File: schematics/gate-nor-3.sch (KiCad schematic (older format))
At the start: 5 parts, among them Q15 NPN

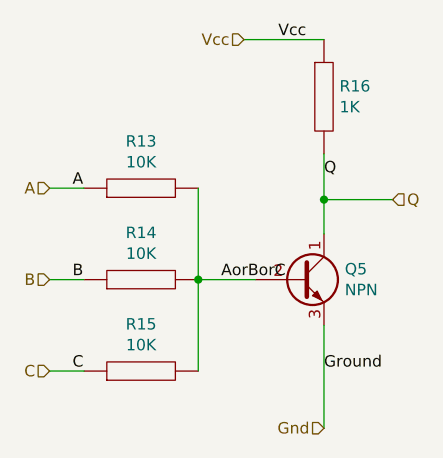
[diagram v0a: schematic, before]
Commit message: Fleshes out basic schematics and some utility software
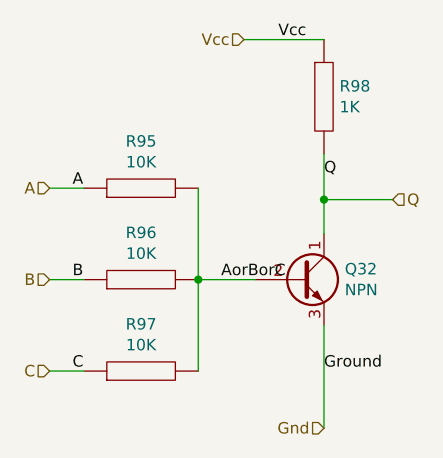
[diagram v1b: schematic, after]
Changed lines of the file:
@@
 EESchema Schematic File Version 4
-LIBS:flip-flop-d-test-cache
 EELAYER 26 0
 EELAYER END
 $Descr A4 11693 8268
 encoding utf-8
-Sheet 20 9
+Sheet 20 50
 Title ""
 Date ""
@@
 AR Path="/5C401646/5C3679F2" Ref="R4"  Part="1"
 AR Path="/5C3FF380/5C403563/5C3679F2" Ref="R16"  Part="1"
-F 0 "R16" H 4268 2546 50  0000 L CNN
+AR Path="/5C4196B1/5C3FF380/5C403563/5C3679F2" Ref="R?"  Part="1"
+AR Path="/5C4199A8/5C403563/5C3679F2" Ref="R?"  Part="1"
+AR Path="/5C41AA0E/5C41AA96/5C3679F2" Ref="R10"  Part="1"
+AR Path="/5C41AA0E/5C41B943/5C3679F2" Ref="R17"  Part="1"
+AR Path="/5C42CE9C/5C41AA0E/5C41AA96/5C3679F2" Ref="R?"  Part="1"
+AR Path="/5C42CE9C/5C41AA0E/5C41B943/5C3679F2" Ref="R?"  Part="1"
+AR Path="/5C42D2B6/5C41AA96/5C3679F2" Ref="R?"  Part="1"
+AR Path="/5C42D2B6/5C41B943/5C3679F2" Ref="R?"  Part="1"
+AR Path="/5C42D642/5C42D9A9/5C41AA96/5C3679F2" Ref="R10"  Part="1"
+AR Path="/5C42D642/5C42D9A9/5C41B943/5C3679F2" Ref="R17"  Part="1"
+AR Path="/5C4309EE/5C42D642/5C42D9A9/5C41AA96/5C3679F2" Ref="R?"  Part="1"
+AR Path="/5C4309EE/5C42D642/5C42D9A9/5C41B943/5C3679F2" Ref="R?"  Part="1"
+AR Path="/5C4310A9/5C42D9A9/5C41AA96/5C3679F2" Ref="R?"  Part="1"
+AR Path="/5C4310A9/5C42D9A9/5C41B943/5C3679F2" Ref="R?"  Part="1"
+AR Path="/5C43173F/5C431DC8/5C42D9A9/5C41AA96/5C3679F2" Ref="R10"  Part="1"
+AR Path="/5C43173F/5C431DC8/5C42D9A9/5C41B943/5C3679F2" Ref="R17"  Part="1"
+AR Path="/5C43173F/5C432023/5C42D9A9/5C41AA96/5C3679F2" Ref="R37"  Part="1"
+AR Path="/5C43173F/5C432023/5C42D9A9/5C41B943/5C3679F2" Ref="R44"  Part="1"
+AR Path="/5C43173F/5C432127/5C42D9A9/5C41AA96/5C3679F2" Ref="R64"  Part="1"
+AR Path="/5C43173F/5C432127/5C42D9A9/5C41B943/5C3679F2" Ref="R71"  Part="1"
+AR Path="/5C43173F/5C4322A0/5C42D9A9/5C41AA96/5C3679F2" Ref="R91"  Part="1"
+AR Path="/5C43173F/5C4322A0/5C42D9A9/5C41B943/5C3679F2" Ref="R98"  Part="1"
+AR Path="/5C43173F/5C4341F5/5C42D9A9/5C41AA96/5C3679F2" Ref="R?"  Part="1"
+AR Path="/5C43173F/5C4341F5/5C42D9A9/5C41B943/5C3679F2" Ref="R?"  Part="1"
+F 0 "R98" H 4268 2546 50  0000 L CNN
 F 1 "1K" H 4268 2455 50  0000 L CNN
 F 2 "" H 4200 2500 50  0001 C CNN
@@
 AR Path="/5C401646/5C3679F9" Ref="R1"  Part="1"
 AR Path="/5C3FF380/5C403563/5C3679F9" Ref="R13"  Part="1"
-F 0 "R13" V 3605 2900 50  0000 C CNN
+AR Path="/5C4196B1/5C3FF380/5C403563/5C3679F9" Ref="R?"  Part="1"
+AR Path="/5C4199A8/5C403563/5C3679F9" Ref="R?"  Part="1"
+AR Path="/5C41AA0E/5C41AA96/5C3679F9" Ref="R7"  Part="1"
+AR Path="/5C41AA0E/5C41B943/5C3679F9" Ref="R14"  Part="1"
+AR Path="/5C42CE9C/5C41AA0E/5C41AA96/5C3679F9" Ref="R?"  Part="1"
+AR Path="/5C42CE9C/5C41AA0E/5C41B943/5C3679F9" Ref="R?"  Part="1"
+AR Path="/5C42D2B6/5C41AA96/5C3679F9" Ref="R?"  Part="1"
+AR Path="/5C42D2B6/5C41B943/5C3679F9" Ref="R?"  Part="1"
+AR Path="/5C42D642/5C42D9A9/5C41AA96/5C3679F9" Ref="R7"  Part="1"
+AR Path="/5C42D642/5C42D9A9/5C41B943/5C3679F9" Ref="R14"  Part="1"
+AR Path="/5C4309EE/5C42D642/5C42D9A9/5C41AA96/5C3679F9" Ref="R?"  Part="1"
+AR Path="/5C4309EE/5C42D642/5C42D9A9/5C41B943/5C3679F9" Ref="R?"  Part="1"
+AR Path="/5C4310A9/5C42D9A9/5C41AA96/5C3679F9" Ref="R?"  Part="1"
+AR Path="/5C4310A9/5C42D9A9/5C41B943/5C3679F9" Ref="R?"  Part="1"
+AR Path="/5C43173F/5C431DC8/5C42D9A9/5C41AA96/5C3679F9" Ref="R7"  Part="1"
+AR Path="/5C43173F/5C431DC8/5C42D9A9/5C41B943/5C3679F9" Ref="R14"  Part="1"
+AR Path="/5C43173F/5C432023/5C42D9A9/5C41AA96/5C3679F9" Ref="R34"  Part="1"
+AR Path="/5C43173F/5C432023/5C42D9A9/5C41B943/5C3679F9" Ref="R41"  Part="1"
+AR Path="/5C43173F/5C432127/5C42D9A9/5C41AA96/5C3679F9" Ref="R61"  Part="1"
+AR Path="/5C43173F/5C432127/5C42D9A9/5C41B943/5C3679F9" Ref="R68"  Part="1"
+AR Path="/5C43173F/5C4322A0/5C42D9A9/5C41AA96/5C3679F9" Ref="R88"  Part="1"
+AR Path="/5C43173F/5C4322A0/5C42D9A9/5C41B943/5C3679F9" Ref="R95"  Part="1"
+AR Path="/5C43173F/5C4341F5/5C42D9A9/5C41AA96/5C3679F9" Ref="R?"  Part="1"
+AR Path="/5C43173F/5C4341F5/5C42D9A9/5C41B943/5C3679F9" Ref="R?"  Part="1"
+F 0 "R95" V 3605 2900 50  0000 C CNN
 F 1 "10K" V 3514 2900 50  0000 C CNN
 F 2 "" H 3400 2900 50  0001 C CNN
@@
 AR Path="/5C401646/5C367A00" Ref="R2"  Part="1"
 AR Path="/5C3FF380/5C403563/5C367A00" Ref="R14"  Part="1"
-F 0 "R14" V 3605 3300 50  0000 C CNN
+AR Path="/5C4196B1/5C3FF380/5C403563/5C367A00" Ref="R?"  Part="1"
+AR Path="/5C4199A8/5C403563/5C367A00" Ref="R?"  Part="1"
+AR Path="/5C41AA0E/5C41AA96/5C367A00" Ref="R8"  Part="1"
+AR Path="/5C41AA0E/5C41B943/5C367A00" Ref="R15"  Part="1"
+AR Path="/5C42CE9C/5C41AA0E/5C41AA96/5C367A00" Ref="R?"  Part="1"
+AR Path="/5C42CE9C/5C41AA0E/5C41B943/5C367A00" Ref="R?"  Part="1"
+AR Path="/5C42D2B6/5C41AA96/5C367A00" Ref="R?"  Part="1"
+AR Path="/5C42D2B6/5C41B943/5C367A00" Ref="R?"  Part="1"
+AR Path="/5C42D642/5C42D9A9/5C41AA96/5C367A00" Ref="R8"  Part="1"
+AR Path="/5C42D642/5C42D9A9/5C41B943/5C367A00" Ref="R15"  Part="1"
+AR Path="/5C4309EE/5C42D642/5C42D9A9/5C41AA96/5C367A00" Ref="R?"  Part="1"
+AR Path="/5C4309EE/5C42D642/5C42D9A9/5C41B943/5C367A00" Ref="R?"  Part="1"
+AR Path="/5C4310A9/5C42D9A9/5C41AA96/5C367A00" Ref="R?"  Part="1"
+AR Path="/5C4310A9/5C42D9A9/5C41B943/5C367A00" Ref="R?"  Part="1"
+AR Path="/5C43173F/5C431DC8/5C42D9A9/5C41AA96/5C367A00" Ref="R8"  Part="1"
+AR Path="/5C43173F/5C431DC8/5C42D9A9/5C41B943/5C367A00" Ref="R15"  Part="1"
+AR Path="/5C43173F/5C432023/5C42D9A9/5C41AA96/5C367A00" Ref="R35"  Part="1"
+AR Path="/5C43173F/5C432023/5C42D9A9/5C41B943/5C367A00" Ref="R42"  Part="1"
+AR Path="/5C43173F/5C432127/5C42D9A9/5C41AA96/5C367A00" Ref="R62"  Part="1"
+AR Path="/5C43173F/5C432127/5C42D9A9/5C41B943/5C367A00" Ref="R69"  Part="1"
+AR Path="/5C43173F/5C4322A0/5C42D9A9/5C41AA96/5C367A00" Ref="R89"  Part="1"
+AR Path="/5C43173F/5C4322A0/5C42D9A9/5C41B943/5C367A00" Ref="R96"  Part="1"
+AR Path="/5C43173F/5C4341F5/5C42D9A9/5C41AA96/5C367A00" Ref="R?"  Part="1"
+AR Path="/5C43173F/5C4341F5/5C42D9A9/5C41B943/5C367A00" Ref="R?"  Part="1"
+F 0 "R96" V 3605 3300 50  0000 C CNN
 F 1 "10K" V 3514 3300 50  0000 C CNN
 F 2 "" H 3400 3300 50  0001 C CNN
@@
 AR Path="/5C401646/5C367A1E" Ref="Q1"  Part="1"
 AR Path="/5C3FF380/5C403563/5C367A1E" Ref="Q5"  Part="1"
-F 0 "Q5" H 4291 3346 50  0000 L CNN
+AR Path="/5C4196B1/5C3FF380/5C403563/5C367A1E" Ref="Q?"  Part="1"
+AR Path="/5C4199A8/5C403563/5C367A1E" Ref="Q?"  Part="1"
+AR Path="/5C41AA0E/5C41AA96/5C367A1E" Ref="Q3"  Part="1"
+AR Path="/5C41AA0E/5C41B943/5C367A1E" Ref="Q5"  Part="1"
+AR Path="/5C42CE9C/5C41AA0E/5C41AA96/5C367A1E" Ref="Q?"  Part="1"
+AR Path="/5C42CE9C/5C41AA0E/5C41B943/5C367A1E" Ref="Q?"  Part="1"
+AR Path="/5C42D2B6/5C41AA96/5C367A1E" Ref="Q?"  Part="1"
+AR Path="/5C42D2B6/5C41B943/5C367A1E" Ref="Q?"  Part="1"
+AR Path="/5C42D642/5C42D9A9/5C41AA96/5C367A1E" Ref="Q3"  Part="1"
+AR Path="/5C42D642/5C42D9A9/5C41B943/5C367A1E" Ref="Q5"  Part="1"
+AR Path="/5C4309EE/5C42D642/5C42D9A9/5C41AA96/5C367A1E" Ref="Q?"  Part="1"
+AR Path="/5C4309EE/5C42D642/5C42D9A9/5C41B943/5C367A1E" Ref="Q?"  Part="1"
+AR Path="/5C4310A9/5C42D9A9/5C41AA96/5C367A1E" Ref="Q?"  Part="1"
+AR Path="/5C4310A9/5C42D9A9/5C41B943/5C367A1E" Ref="Q?"  Part="1"
+AR Path="/5C43173F/5C431DC8/5C42D9A9/5C41AA96/5C367A1E" Ref="Q3"  Part="1"
+AR Path="/5C43173F/5C431DC8/5C42D9A9/5C41B943/5C367A1E" Ref="Q5"  Part="1"
+AR Path="/5C43173F/5C432023/5C42D9A9/5C41AA96/5C367A1E" Ref="Q12"  Part="1"
+AR Path="/5C43173F/5C432023/5C42D9A9/5C41B943/5C367A1E" Ref="Q14"  Part="1"
+AR Path="/5C43173F/5C432127/5C42D9A9/5C41AA96/5C367A1E" Ref="Q21"  Part="1"
+AR Path="/5C43173F/5C432127/5C42D9A9/5C41B943/5C367A1E" Ref="Q23"  Part="1"
+AR Path="/5C43173F/5C4322A0/5C42D9A9/5C41AA96/5C367A1E" Ref="Q30"  Part="1"
+AR Path="/5C43173F/5C4322A0/5C42D9A9/5C41B943/5C367A1E" Ref="Q32"  Part="1"
+AR Path="/5C43173F/5C4341F5/5C42D9A9/5C41AA96/5C367A1E" Ref="Q?"  Part="1"
+AR Path="/5C43173F/5C4341F5/5C42D9A9/5C41B943/5C367A1E" Ref="Q?"  Part="1"
+F 0 "Q32" H 4291 3346 50  0000 L CNN
 F 1 "NPN" H 4291 3255 50  0000 L CNN
 F 2 "Package_TO_SOT_THT:TO-92_Inline" H 4300 3225 50  0001 L CIN
@@
 AR Path="/5C401646/5C367BB4" Ref="R3"  Part="1"
 AR Path="/5C3FF380/5C403563/5C367BB4" Ref="R15"  Part="1"
-F 0 "R15" V 3605 3700 50  0000 C CNN
+AR Path="/5C4196B1/5C3FF380/5C403563/5C367BB4" Ref="R?"  Part="1"
+AR Path="/5C4199A8/5C403563/5C367BB4" Ref="R?"  Part="1"
+AR Path="/5C41AA0E/5C41AA96/5C367BB4" Ref="R9"  Part="1"
+AR Path="/5C41AA0E/5C41B943/5C367BB4" Ref="R16"  Part="1"
+AR Path="/5C42CE9C/5C41AA0E/5C41AA96/5C367BB4" Ref="R?"  Part="1"
+AR Path="/5C42CE9C/5C41AA0E/5C41B943/5C367BB4" Ref="R?"  Part="1"
+AR Path="/5C42D2B6/5C41AA96/5C367BB4" Ref="R?"  Part="1"
+AR Path="/5C42D2B6/5C41B943/5C367BB4" Ref="R?"  Part="1"
+AR Path="/5C42D642/5C42D9A9/5C41AA96/5C367BB4" Ref="R9"  Part="1"
+AR Path="/5C42D642/5C42D9A9/5C41B943/5C367BB4" Ref="R16"  Part="1"
+AR Path="/5C4309EE/5C42D642/5C42D9A9/5C41AA96/5C367BB4" Ref="R?"  Part="1"
+AR Path="/5C4309EE/5C42D642/5C42D9A9/5C41B943/5C367BB4" Ref="R?"  Part="1"
+AR Path="/5C4310A9/5C42D9A9/5C41AA96/5C367BB4" Ref="R?"  Part="1"
+AR Path="/5C4310A9/5C42D9A9/5C41B943/5C367BB4" Ref="R?"  Part="1"
+AR Path="/5C43173F/5C431DC8/5C42D9A9/5C41AA96/5C367BB4" Ref="R9"  Part="1"
+AR Path="/5C43173F/5C431DC8/5C42D9A9/5C41B943/5C367BB4" Ref="R16"  Part="1"
+AR Path="/5C43173F/5C432023/5C42D9A9/5C41AA96/5C367BB4" Ref="R36"  Part="1"
+AR Path="/5C43173F/5C432023/5C42D9A9/5C41B943/5C367BB4" Ref="R43"  Part="1"
+AR Path="/5C43173F/5C432127/5C42D9A9/5C41AA96/5C367BB4" Ref="R63"  Part="1"
+AR Path="/5C43173F/5C432127/5C42D9A9/5C41B943/5C367BB4" Ref="R70"  Part="1"
+AR Path="/5C43173F/5C4322A0/5C42D9A9/5C41AA96/5C367BB4" Ref="R90"  Part="1"
+AR Path="/5C43173F/5C4322A0/5C42D9A9/5C41B943/5C367BB4" Ref="R97"  Part="1"
+AR Path="/5C43173F/5C4341F5/5C42D9A9/5C41AA96/5C367BB4" Ref="R?"  Part="1"
+AR Path="/5C43173F/5C4341F5/5C42D9A9/5C41B943/5C367BB4" Ref="R?"  Part="1"
+F 0 "R97" V 3605 3700 50  0000 C CNN
 F 1 "10K" V 3514 3700 50  0000 C CNN
 F 2 "" H 3400 3700 50  0001 C CNN

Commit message: Adds some tests for and-2, nor-2, nor-3
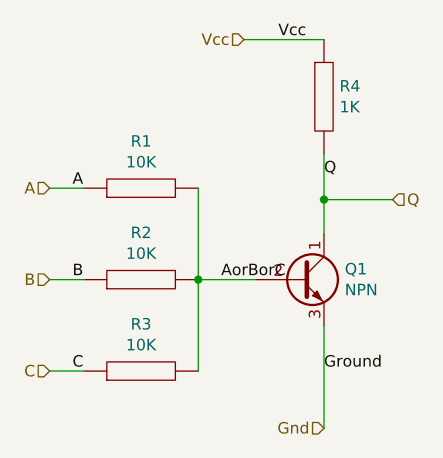
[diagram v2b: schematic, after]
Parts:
- renumbered Q15 to Q1, R41 to R1, R42 to R2, R43 to R3, R44 to R4

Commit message: Can now automate transient analysis
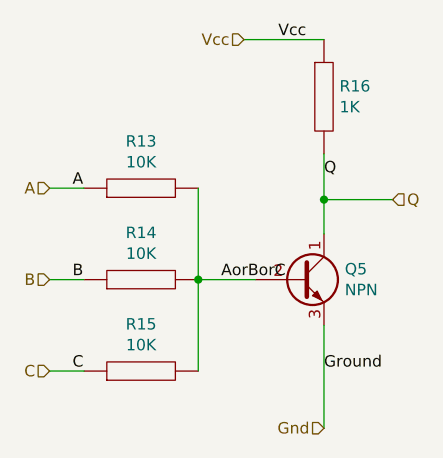
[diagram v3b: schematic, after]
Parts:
- renumbered Q1 to Q5, R1 to R13, R2 to R14, R3 to R15, R4 to R16
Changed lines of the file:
@@
 EESchema Schematic File Version 4
-LIBS:gate-nor-3-test-cache
+LIBS:flip-flop-d-test-cache
 EELAYER 26 0
 EELAYER END
 $Descr A4 11693 8268
 encoding utf-8
-Sheet 20 2
+Sheet 20 9
 Title ""
 Date ""
@@
 AR Path="/5C36C049/5C36C553/5C368E7F/5C3679F2" Ref="R?"  Part="1"
 AR Path="/5C36C049/5C36C921/5C368E7F/5C3679F2" Ref="R?"  Part="1"
-AR Path="/5C401646/5C3679F2" Ref="R4"  Part="1"
-AR Path="/5C3FF380/5C403563/5C3679F2" Ref="R?"  Part="1"
+AR Path="/5C401646/5C3679F2" Ref="R?"  Part="1"
+AR Path="/5C3FF380/5C403563/5C3679F2" Ref="R16"  Part="1"
 AR Path="/5C4196B1/5C3FF380/5C403563/5C3679F2" Ref="R?"  Part="1"
 AR Path="/5C4199A8/5C403563/5C3679F2" Ref="R?"  Part="1"
@@
 AR Path="/5C43173F/5C4341F5/5C42D9A9/5C41AA96/5C3679F2" Ref="R?"  Part="1"
 AR Path="/5C43173F/5C4341F5/5C42D9A9/5C41B943/5C3679F2" Ref="R?"  Part="1"
-F 0 "R4" H 4268 2546 50  0000 L CNN
+F 0 "R16" H 4268 2546 50  0000 L CNN
 F 1 "1K" H 4268 2455 50  0000 L CNN
 F 2 "" H 4200 2500 50  0001 C CNN
@@
 AR Path="/5C36C049/5C36C553/5C368E7F/5C3679F9" Ref="R?"  Part="1"
 AR Path="/5C36C049/5C36C921/5C368E7F/5C3679F9" Ref="R?"  Part="1"
-AR Path="/5C401646/5C3679F9" Ref="R1"  Part="1"
-AR Path="/5C3FF380/5C403563/5C3679F9" Ref="R?"  Part="1"
+AR Path="/5C401646/5C3679F9" Ref="R?"  Part="1"
+AR Path="/5C3FF380/5C403563/5C3679F9" Ref="R13"  Part="1"
 AR Path="/5C4196B1/5C3FF380/5C403563/5C3679F9" Ref="R?"  Part="1"
 AR Path="/5C4199A8/5C403563/5C3679F9" Ref="R?"  Part="1"
@@
 AR Path="/5C43173F/5C4341F5/5C42D9A9/5C41AA96/5C3679F9" Ref="R?"  Part="1"
 AR Path="/5C43173F/5C4341F5/5C42D9A9/5C41B943/5C3679F9" Ref="R?"  Part="1"
-F 0 "R1" V 3605 2900 50  0000 C CNN
+F 0 "R13" V 3605 2900 50  0000 C CNN
 F 1 "10K" V 3514 2900 50  0000 C CNN
 F 2 "" H 3400 2900 50  0001 C CNN
@@
 AR Path="/5C36C049/5C36C553/5C368E7F/5C367A00" Ref="R?"  Part="1"
 AR Path="/5C36C049/5C36C921/5C368E7F/5C367A00" Ref="R?"  Part="1"
-AR Path="/5C401646/5C367A00" Ref="R2"  Part="1"
-AR Path="/5C3FF380/5C403563/5C367A00" Ref="R?"  Part="1"
+AR Path="/5C401646/5C367A00" Ref="R?"  Part="1"
+AR Path="/5C3FF380/5C403563/5C367A00" Ref="R14"  Part="1"
 AR Path="/5C4196B1/5C3FF380/5C403563/5C367A00" Ref="R?"  Part="1"
 AR Path="/5C4199A8/5C403563/5C367A00" Ref="R?"  Part="1"
@@
 AR Path="/5C43173F/5C4341F5/5C42D9A9/5C41AA96/5C367A00" Ref="R?"  Part="1"
 AR Path="/5C43173F/5C4341F5/5C42D9A9/5C41B943/5C367A00" Ref="R?"  Part="1"
-F 0 "R2" V 3605 3300 50  0000 C CNN
+F 0 "R14" V 3605 3300 50  0000 C CNN
 F 1 "10K" V 3514 3300 50  0000 C CNN
 F 2 "" H 3400 3300 50  0001 C CNN
@@
 AR Path="/5C36C049/5C36C553/5C368E7F/5C367A1E" Ref="Q?"  Part="1"
 AR Path="/5C36C049/5C36C921/5C368E7F/5C367A1E" Ref="Q?"  Part="1"
-AR Path="/5C401646/5C367A1E" Ref="Q1"  Part="1"
-AR Path="/5C3FF380/5C403563/5C367A1E" Ref="Q?"  Part="1"
+AR Path="/5C401646/5C367A1E" Ref="Q?"  Part="1"
+AR Path="/5C3FF380/5C403563/5C367A1E" Ref="Q5"  Part="1"
 AR Path="/5C4196B1/5C3FF380/5C403563/5C367A1E" Ref="Q?"  Part="1"
 AR Path="/5C4199A8/5C403563/5C367A1E" Ref="Q?"  Part="1"
@@
 AR Path="/5C43173F/5C4341F5/5C42D9A9/5C41AA96/5C367A1E" Ref="Q?"  Part="1"
 AR Path="/5C43173F/5C4341F5/5C42D9A9/5C41B943/5C367A1E" Ref="Q?"  Part="1"
-F 0 "Q1" H 4291 3346 50  0000 L CNN
+F 0 "Q5" H 4291 3346 50  0000 L CNN
 F 1 "NPN" H 4291 3255 50  0000 L CNN
 F 2 "Package_TO_SOT_THT:TO-92_Inline" H 4300 3225 50  0001 L CIN
@@
 AR Path="/5C36C049/5C36C553/5C368E7F/5C367BB4" Ref="R?"  Part="1"
 AR Path="/5C36C049/5C36C921/5C368E7F/5C367BB4" Ref="R?"  Part="1"
-AR Path="/5C401646/5C367BB4" Ref="R3"  Part="1"
-AR Path="/5C3FF380/5C403563/5C367BB4" Ref="R?"  Part="1"
+AR Path="/5C401646/5C367BB4" Ref="R?"  Part="1"
+AR Path="/5C3FF380/5C403563/5C367BB4" Ref="R15"  Part="1"
 AR Path="/5C4196B1/5C3FF380/5C403563/5C367BB4" Ref="R?"  Part="1"
 AR Path="/5C4199A8/5C403563/5C367BB4" Ref="R?"  Part="1"
@@
 AR Path="/5C43173F/5C4341F5/5C42D9A9/5C41AA96/5C367BB4" Ref="R?"  Part="1"
 AR Path="/5C43173F/5C4341F5/5C42D9A9/5C41B943/5C367BB4" Ref="R?"  Part="1"
-F 0 "R3" V 3605 3700 50  0000 C CNN
+F 0 "R15" V 3605 3700 50  0000 C CNN
 F 1 "10K" V 3514 3700 50  0000 C CNN
 F 2 "" H 3400 3700 50  0001 C CNN
